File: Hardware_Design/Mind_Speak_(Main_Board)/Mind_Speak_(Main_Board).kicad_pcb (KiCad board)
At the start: 4 copper layers, 70 x 55 mm, 87 parts, among them J1 microSD, J2 Conn_01x04_Pin, J3 Conn_02x13_Odd_Even, J4 Conn_01x04_Pin, J5 Conn_01x08_Pin, J6 Conn_01x02_Pin, J7 Conn_01x05_Pin, J8 Conn_01x05_Pin, P1 S2B-PH-SM4-TB_LF__SN_, SW1 SW_MEC_5E, SW2 SW_MEC_5E, SW3 SW_MEC_5E, U1 SN74LVC1G32DCKR, U10 PIC32MX250F128B-I_SS, U2 TPS60403DBV, U3 CDBU0130L, U4 LIS3DH, U5 LP5907MFX-3.3, U6 TPS72325DBVR, U7 TLV70025_SOT23-5, U8 ADS1299, U9 NINA-B30x, Y1 ABMM2-8.000MHZ-E2-T

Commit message: Last Edit In Layout Of Main Board
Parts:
- added G***: LOGO, Graphics:MindSpeak_Logo, F.Cu at (103.0, 86.4)
- added G***: LOGO, Graphics:Mo3_Tech_Logo, F.Cu at (126.2, 55.6)
- moved J4 40.8 mm to (100.2, 96.4), turned to -90 degrees
- moved J2 36.3 mm to (71.7, 67.2), turned to 19.29 degrees
- moved R4 0.70 mm to (83.2, 77.7)
- moved C40 0.63 mm to (83.2, 88.6), turned to 90 degrees
- moved Y1 0.41 mm to (81.4, 84.2)
- moved C1 0.40 mm to (116.0, 78.1)
- moved C2 0.40 mm to (115.4, 79.4)
- moved SW2 0.40 mm to (84.5, 74.3)
- moved U4 0.40 mm to (112.4, 79.1)
- moved U1 0.30 mm to (107.9, 79.1), turned to 180 degrees
- moved J5 0.30 mm to (72.4, 56.2)
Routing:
- net NINA_PWR: track 5.03 -> 59.5 mm, vias 0 -> 1
- net SCLK: track 12.3 -> 59.2 mm, vias 0 -> 3
- net MISO: track 29.3 -> 70.5 mm, vias 2 -> 5
- net MOSI: track 9.57 -> 47.4 mm, vias 1 -> 3
- net INT1: track 0.00 -> 34.8 mm, vias 0 -> 2
- net RESET: track 9.99 -> 41.7 mm, vias 0 -> 2
- net DRDY: track 0.00 -> 30.7 mm
- net CLK: track 0.00 -> 28.1 mm, vias 0 -> 1
- net /TXD: track 0.00 -> 27.0 mm, vias 0 -> 2
- net /MCLR: track 7.83 -> 33.8 mm, vias 0 -> 2
- net CS2: track 0.00 -> 23.9 mm, vias 0 -> 1
- net /RXD: track 0.00 -> 23.8 mm, vias 0 -> 4
- net CS4: track 0.00 -> 21.9 mm, vias 0 -> 2
- net /PGED: track 13.6 -> 32.4 mm, vias 0 -> 1
- net /D18: track 0.00 -> 17.6 mm
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
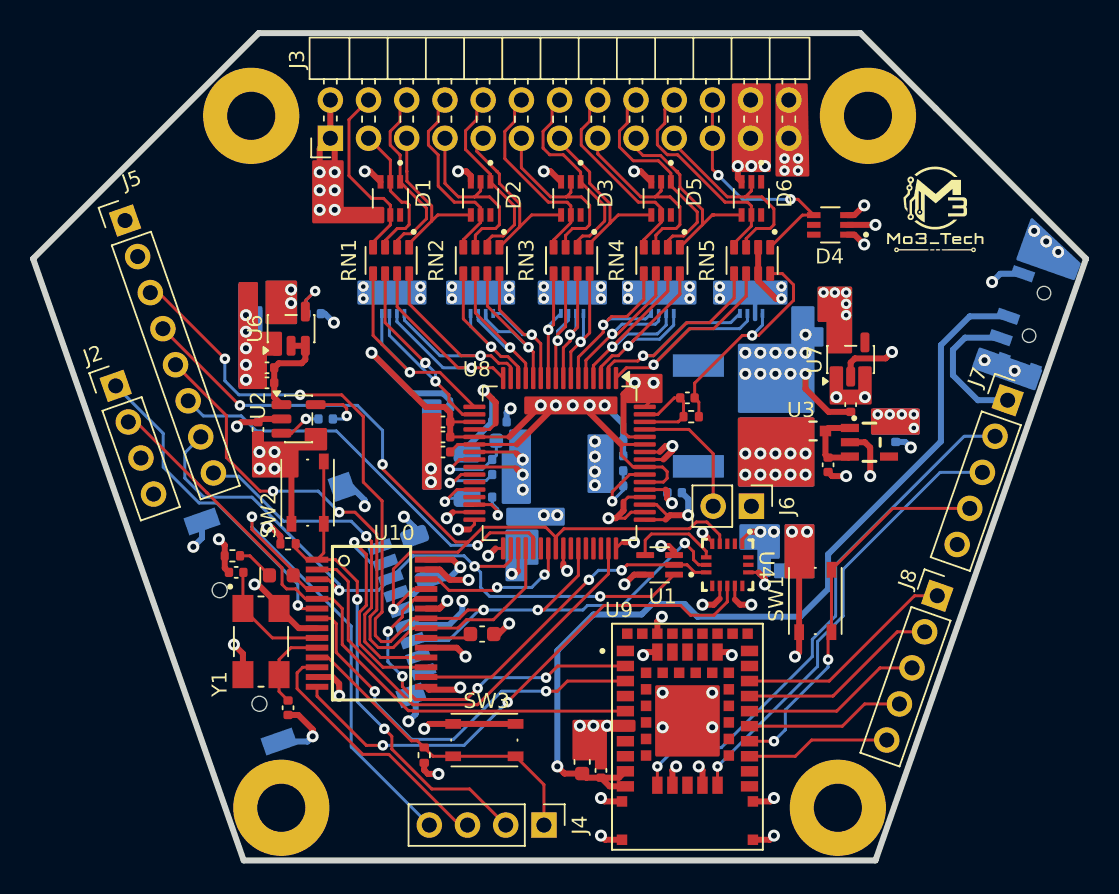
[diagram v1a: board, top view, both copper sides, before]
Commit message: Edit in Dongle/Main Boards
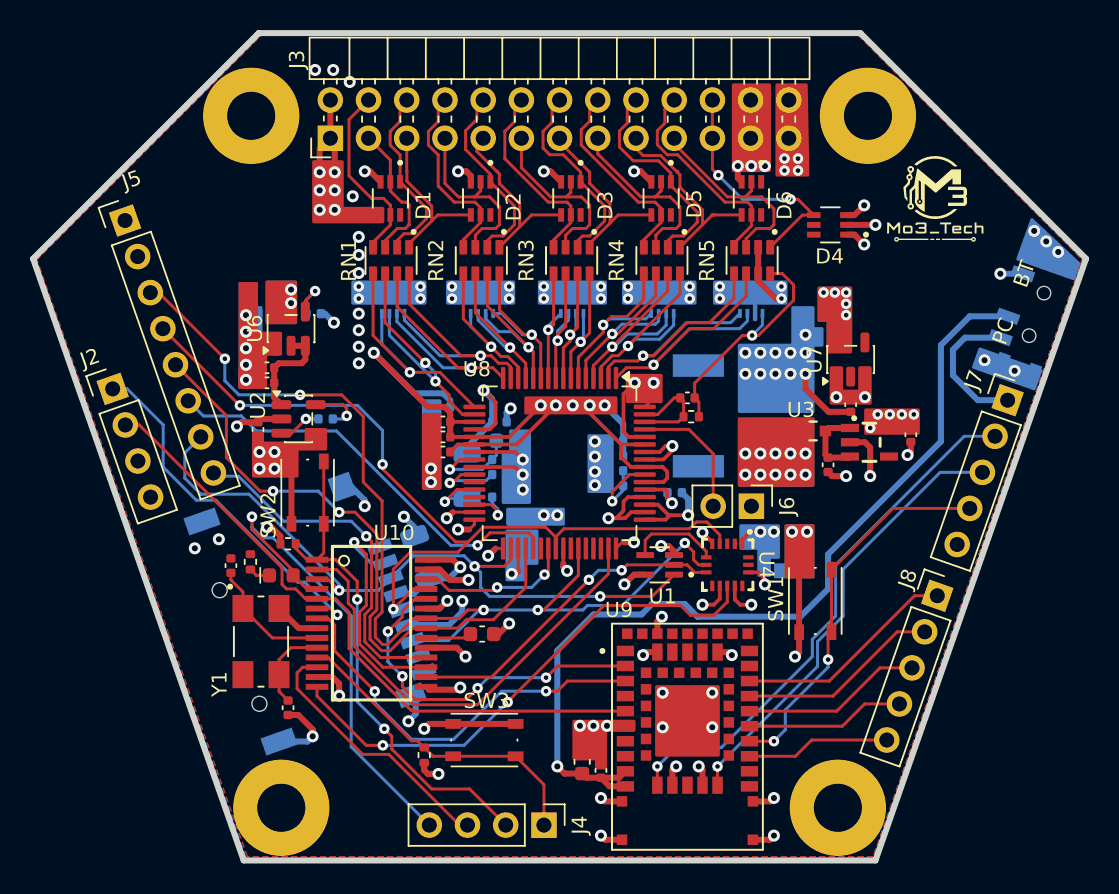
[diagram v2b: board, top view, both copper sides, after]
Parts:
- C9: moved to F.Cu
- moved G*** 6.17 mm to (108.8, 88.4)
- moved R2 1.26 mm to (80.7, 78.9), turned to -90 degrees
- moved C9 1.00 mm to (124.6, 70.5)
- moved G*** 0.70 mm to (126.2, 54.9)
- moved C39 0.57 mm to (79.4, 79.2), turned to -90 degrees
- moved J2 0.28 mm to (71.5, 67.4)
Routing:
- net GNDA: track 114.0 -> 100.8 mm, vias 106 -> 114
- net /D13: track 21.7 -> 24.3 mm
- net Net-(D7-K): track 2.49 -> 1.42 mm
- net +3V3: track 41.1 -> 40.3 mm
- net /PGEC: track 43.1 -> 43.7 mm
- added copper zone on B.Cu, net GNDA
- added copper zone on F.Cu, net GNDA
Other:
- board text added: "+"
- board text added: "-"
- board text added: "BIAS_INV"
- board text added: "BOOT_EN"
- board text added: "BT"
- board text added: "D18"
- board text added: "GND"
- board text added: "GPIO_18"
- board text added: "GPIO_20"
- board text added: "GPIO_21"
- board text added: "GPIO_22"
- board text added: "GPIO_23"
- board text added: "MCLR"
- board text added: "NINA_RST"
- board text added: "NINA_VCC"
- board text added: "PC"
- board text added: "PGED"
- board text added: "SWD_CLK"
- board text added: "SWD_IO"

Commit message: Last Update and Updated the BOM List
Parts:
- moved J5 0.20 mm to (72.6, 56.2)
- moved J2 0.14 mm to (71.4, 67.5)
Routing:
- net SCLK: track 59.2 -> 59.9 mm
- net /PGEC: track 43.7 -> 43.2 mm
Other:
- board text added: "+2.5VA"
- board text added: "+3V3"
- board text added: "-2.5VA"
- board text added: "3V3"
- board text added: "BIAS"
- board text added: "CLK"
- board text added: "CS2"
- board text added: "D13"
- board text added: "MISO"
- board text added: "MOSI"
- board text added: "P1N"
- board text added: "P2N"
- board text added: "P3N"
- board text added: "P4N"
- board text added: "P5N"
- board text added: "P6N"
- board text added: "P7N"
- board text added: "P8N"
- board text added: "PG"
- board text added: "PIC_MCLR"
- board text added: "RESET"
- board text added: "SCLK"
- board text added: "SRB2"
